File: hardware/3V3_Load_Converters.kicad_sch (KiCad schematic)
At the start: 78 parts, among them J23 61300311121, J24 61300311121, Q28 EPC2016C, Q29 EPC2016C, Q30 EPC2016C, Q31 EPC2016C, Q8 SI2302DDS-T1-GE3, Q9 SI2302DDS-T1-GE3, U21 INA199C3DCKR, U30 LTC3833EUDC-TRPBF, U31 LTC3833EUDC-TRPBF

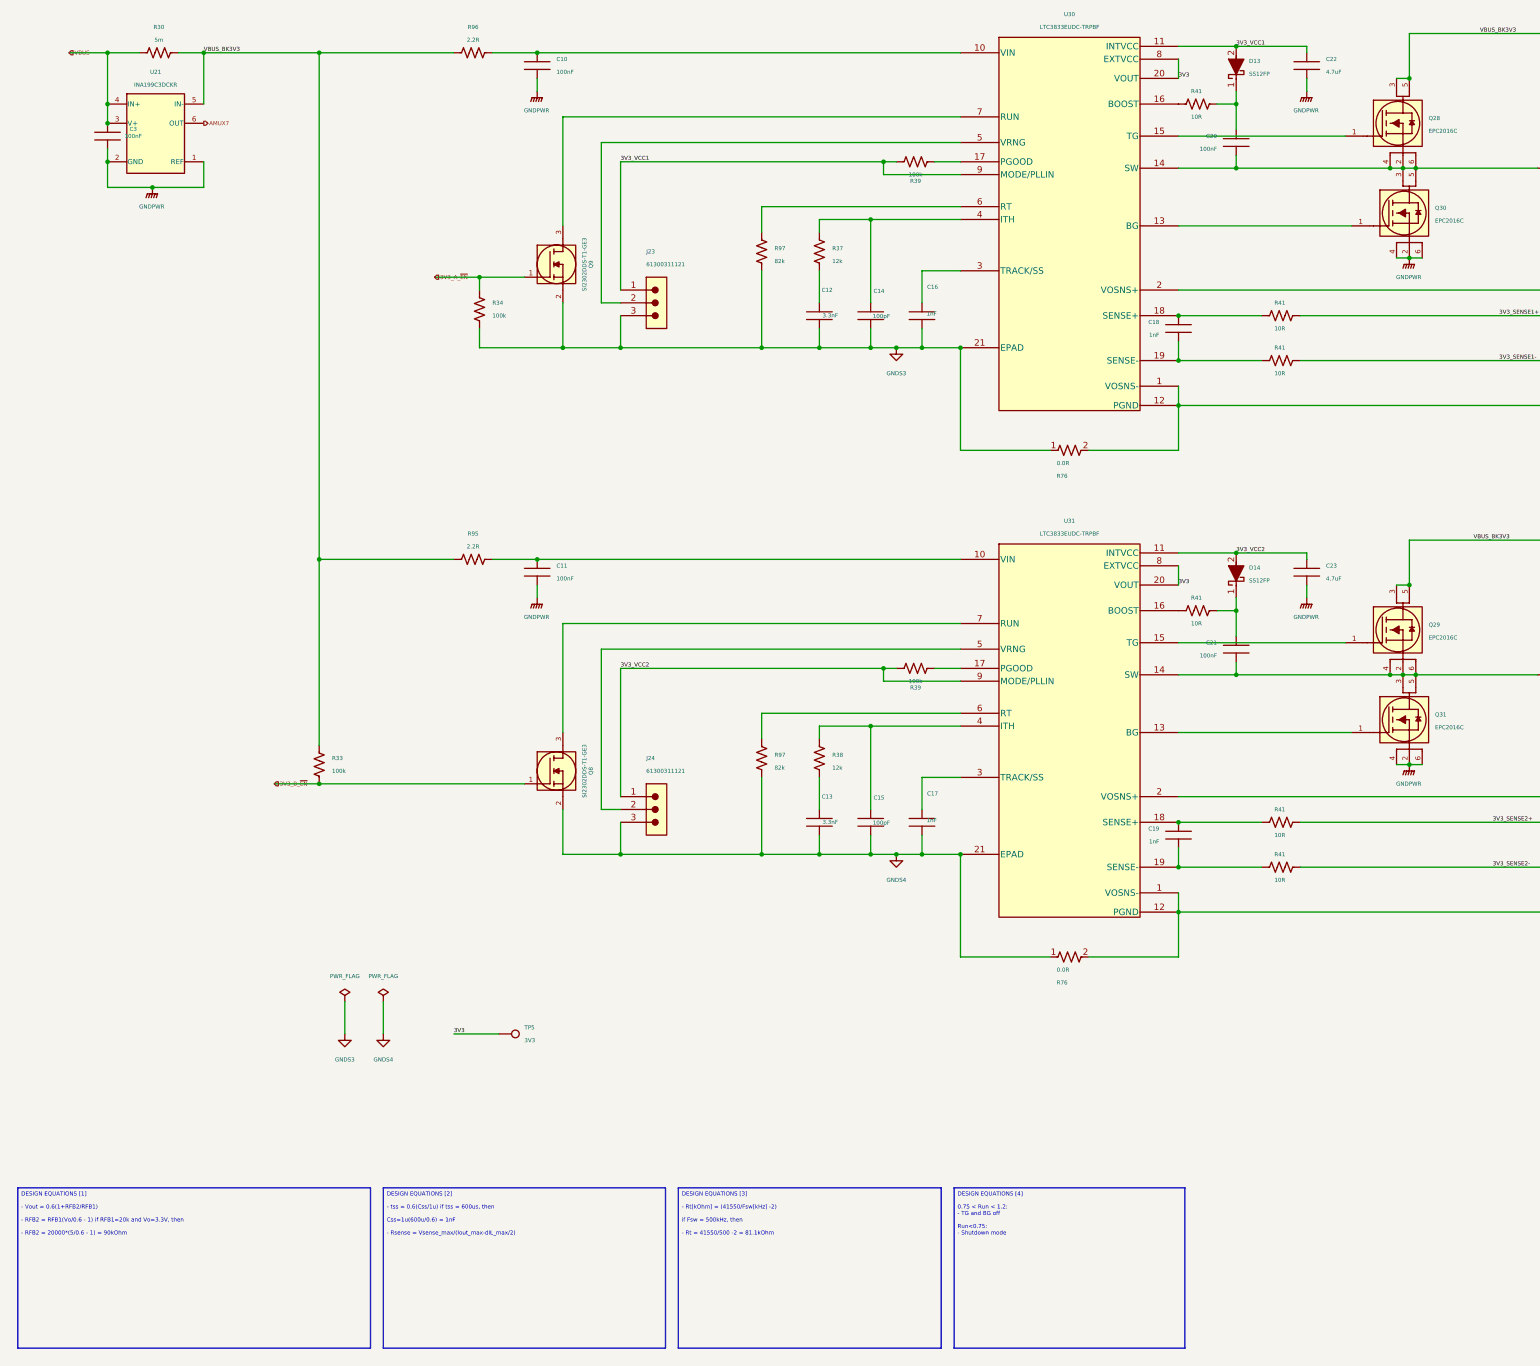
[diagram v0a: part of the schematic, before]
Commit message: hardware: Increasing the readability of the schematic and adding a table with the revision history
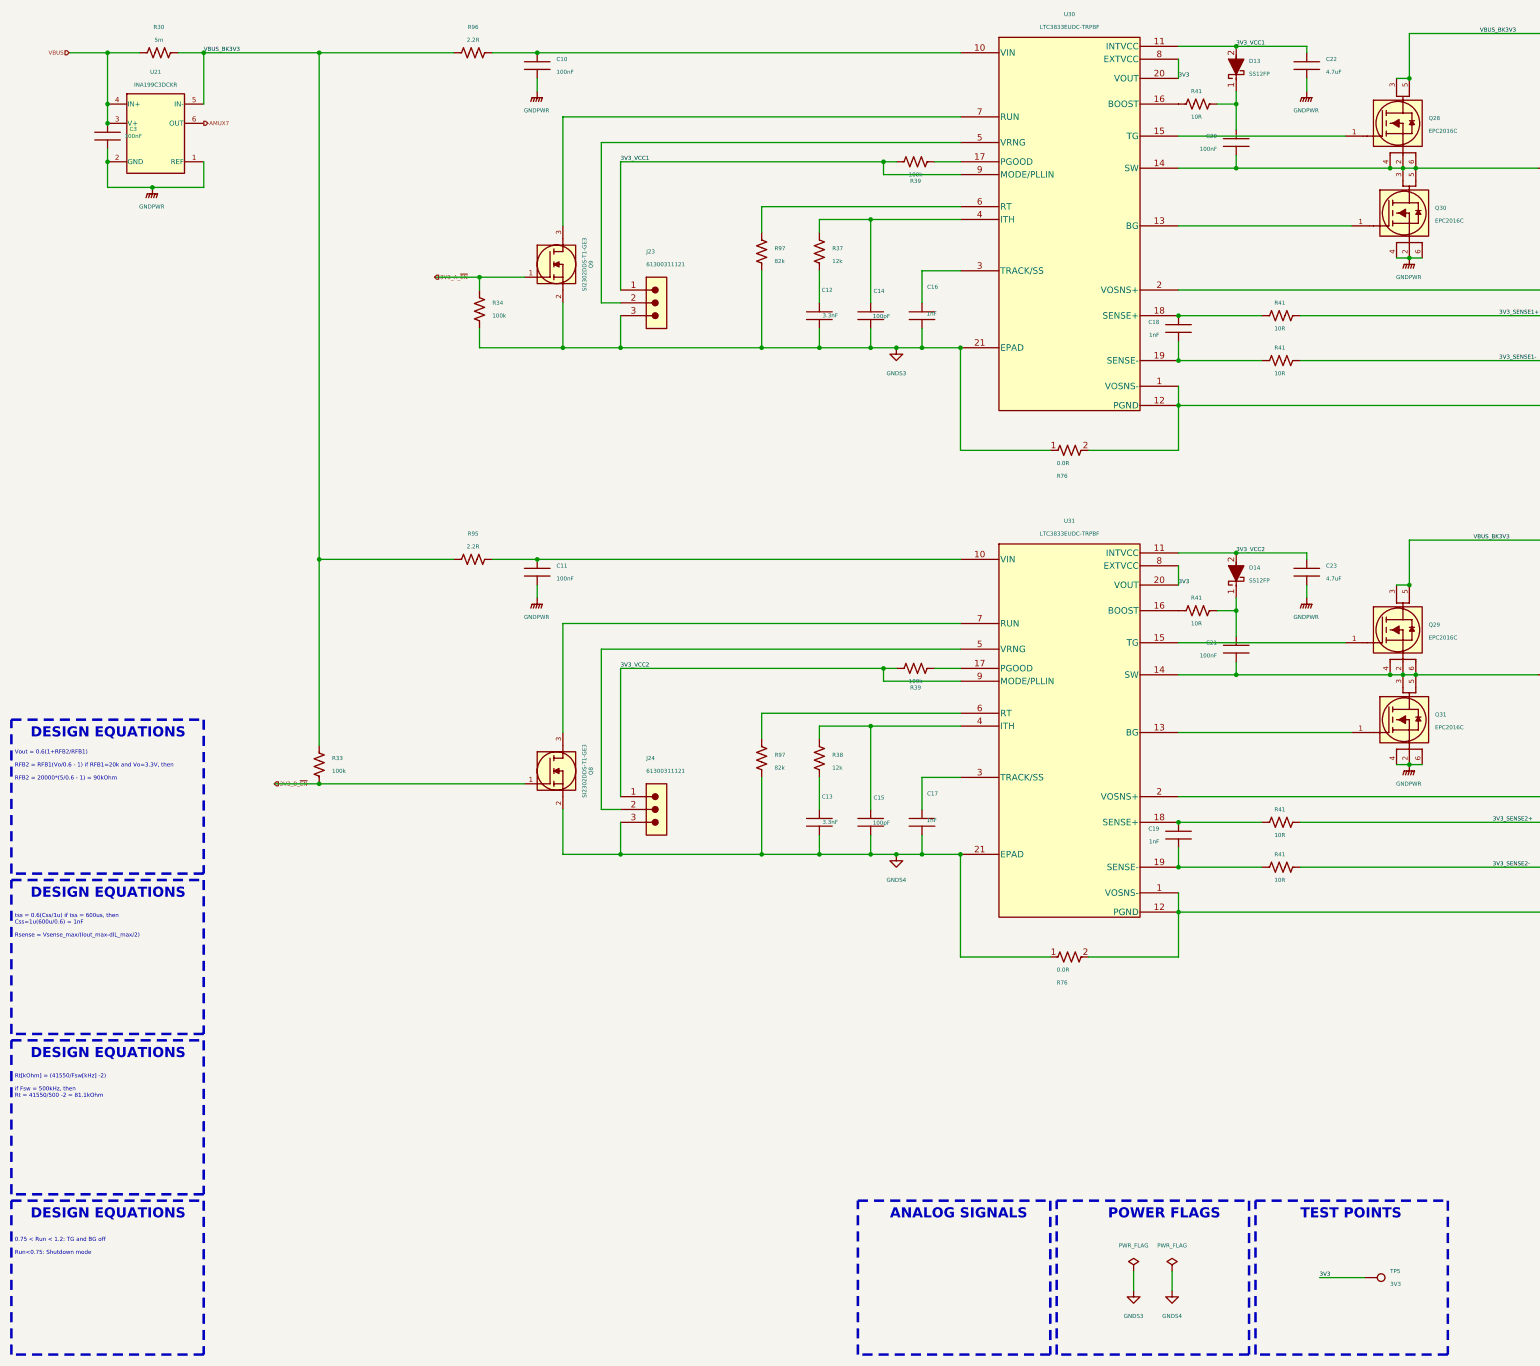
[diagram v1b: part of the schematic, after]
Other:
- note added: "ANALOG SIGNALS"
- note added: "DESIGN EQUATIONS"
- note added: "POWER FLAGS"
- note added: "TEST POINTS"
- moved on the sheet: TP5

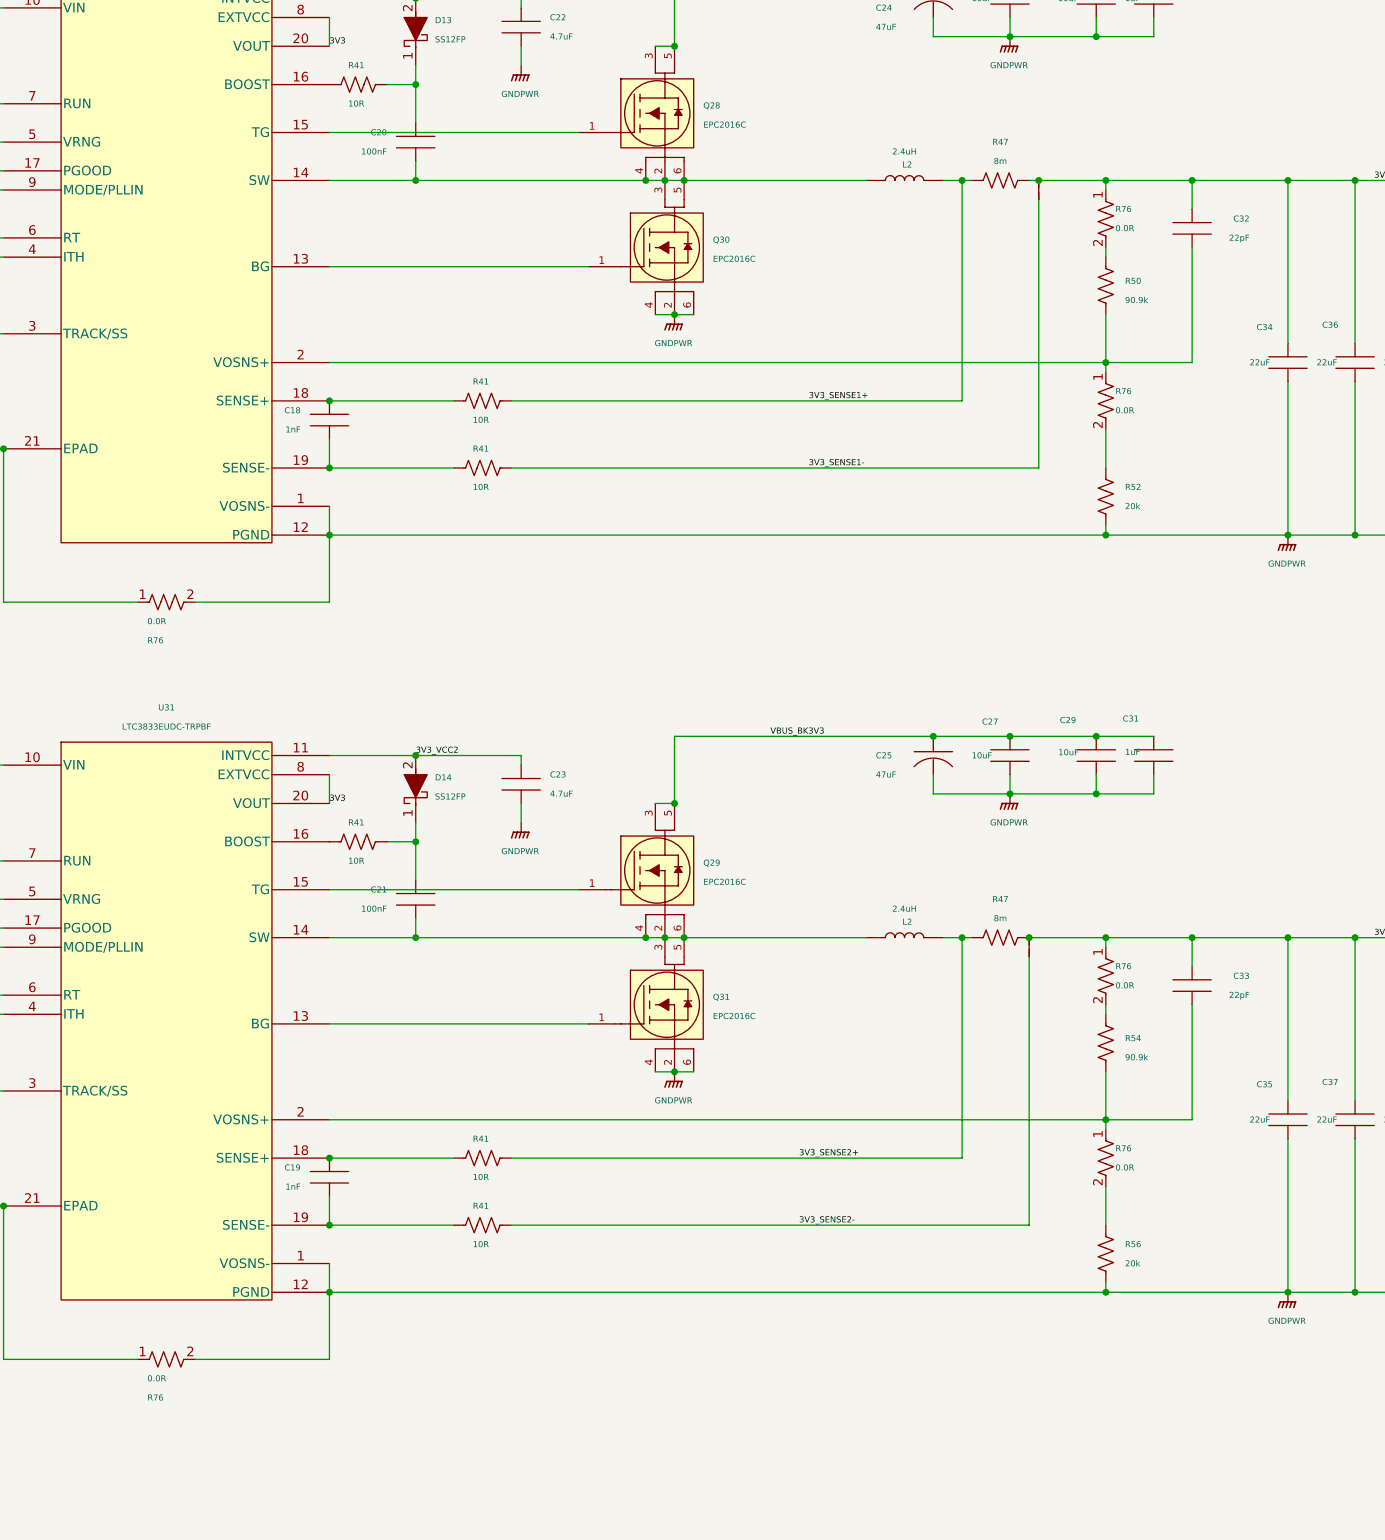
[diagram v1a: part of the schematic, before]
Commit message: hardware: Improving the readability of schematic
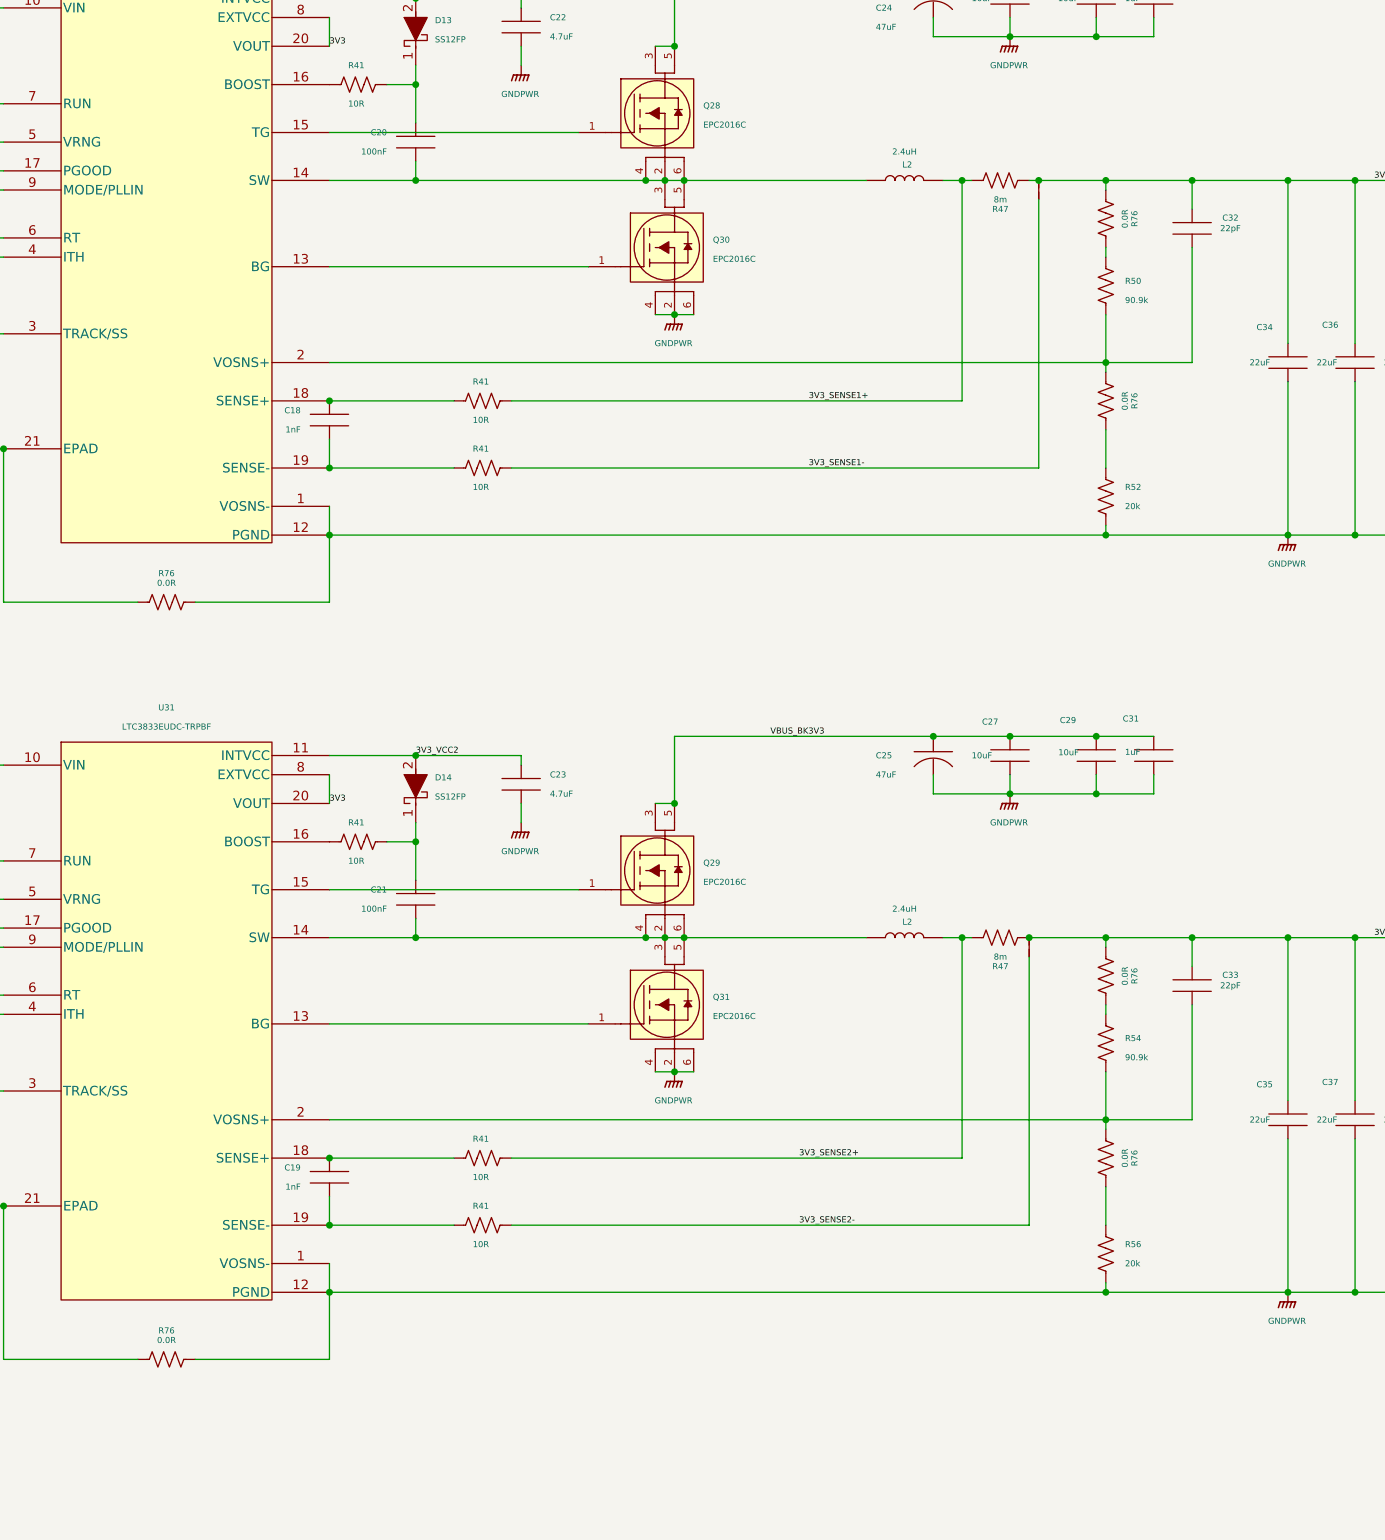
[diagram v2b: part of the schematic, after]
